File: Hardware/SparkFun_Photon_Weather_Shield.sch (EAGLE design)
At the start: 43 parts, among them U1 3.3V MIC5219, U2 HTU21D, U3 MPL3115A2LGA8

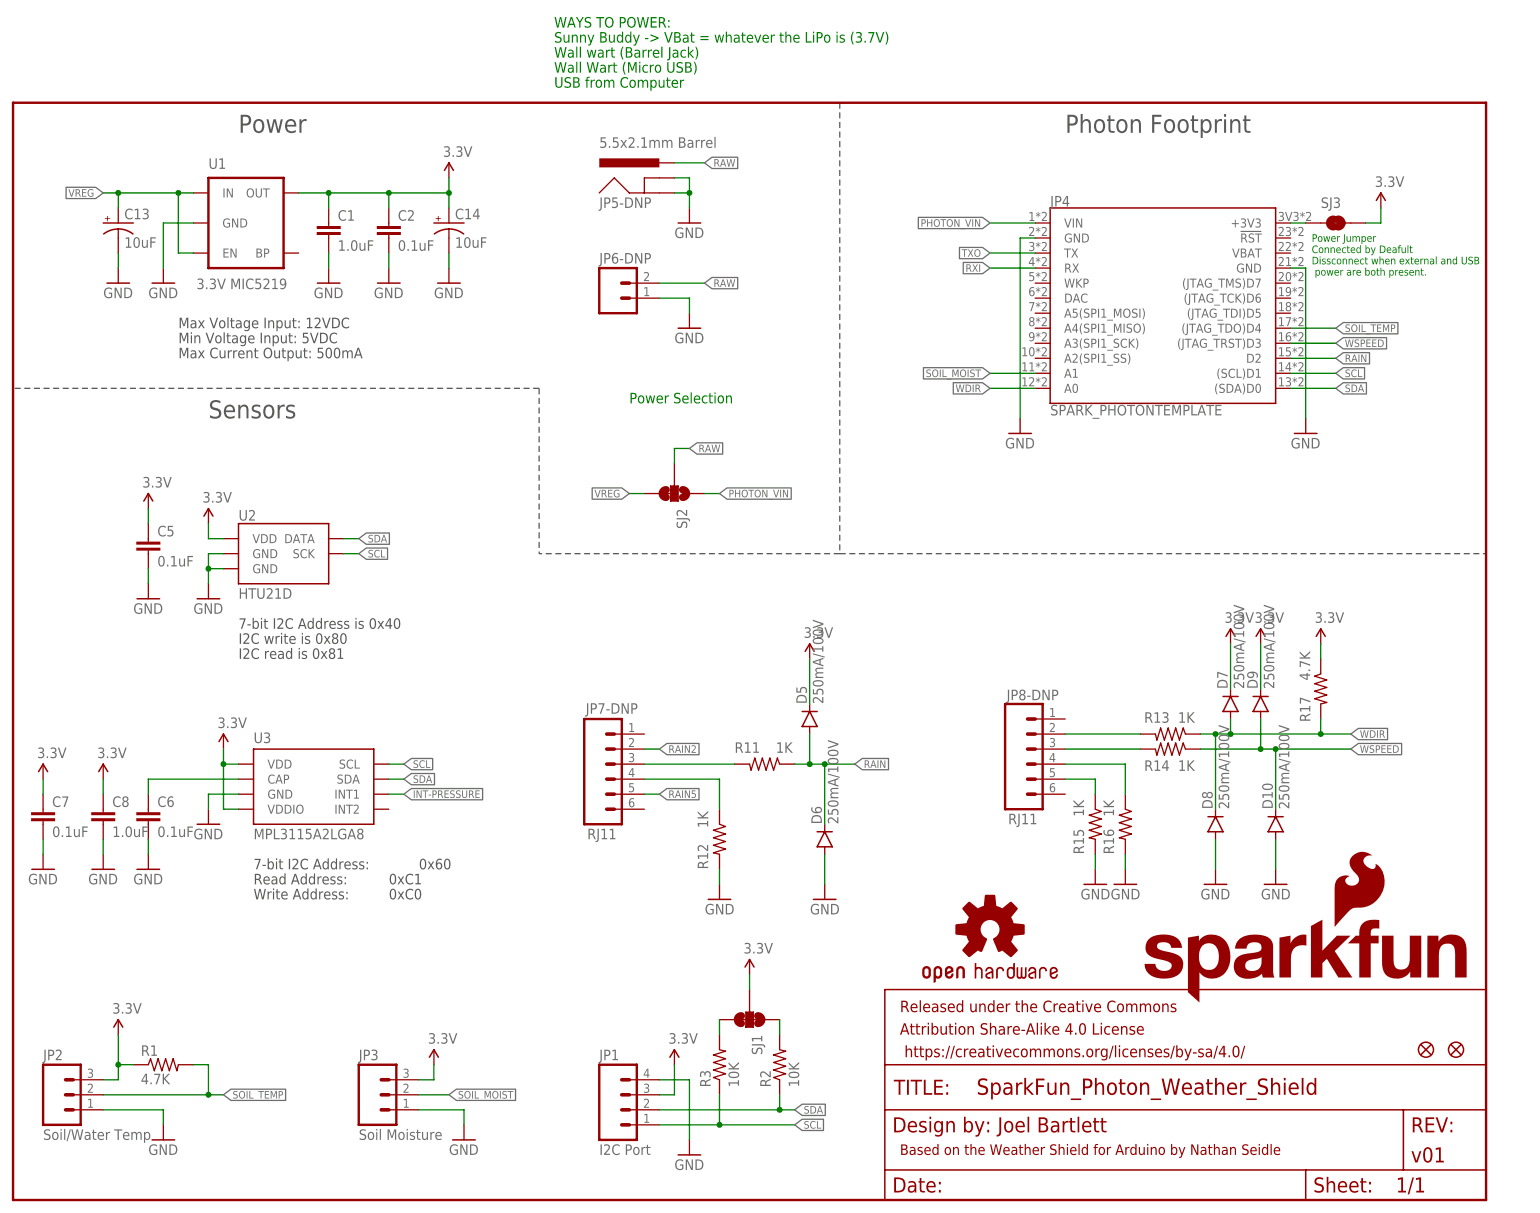
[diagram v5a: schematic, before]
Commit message: Ready for Reds
Added USART port, changed soil moisture vcc to D5, minor silk and route
changes.
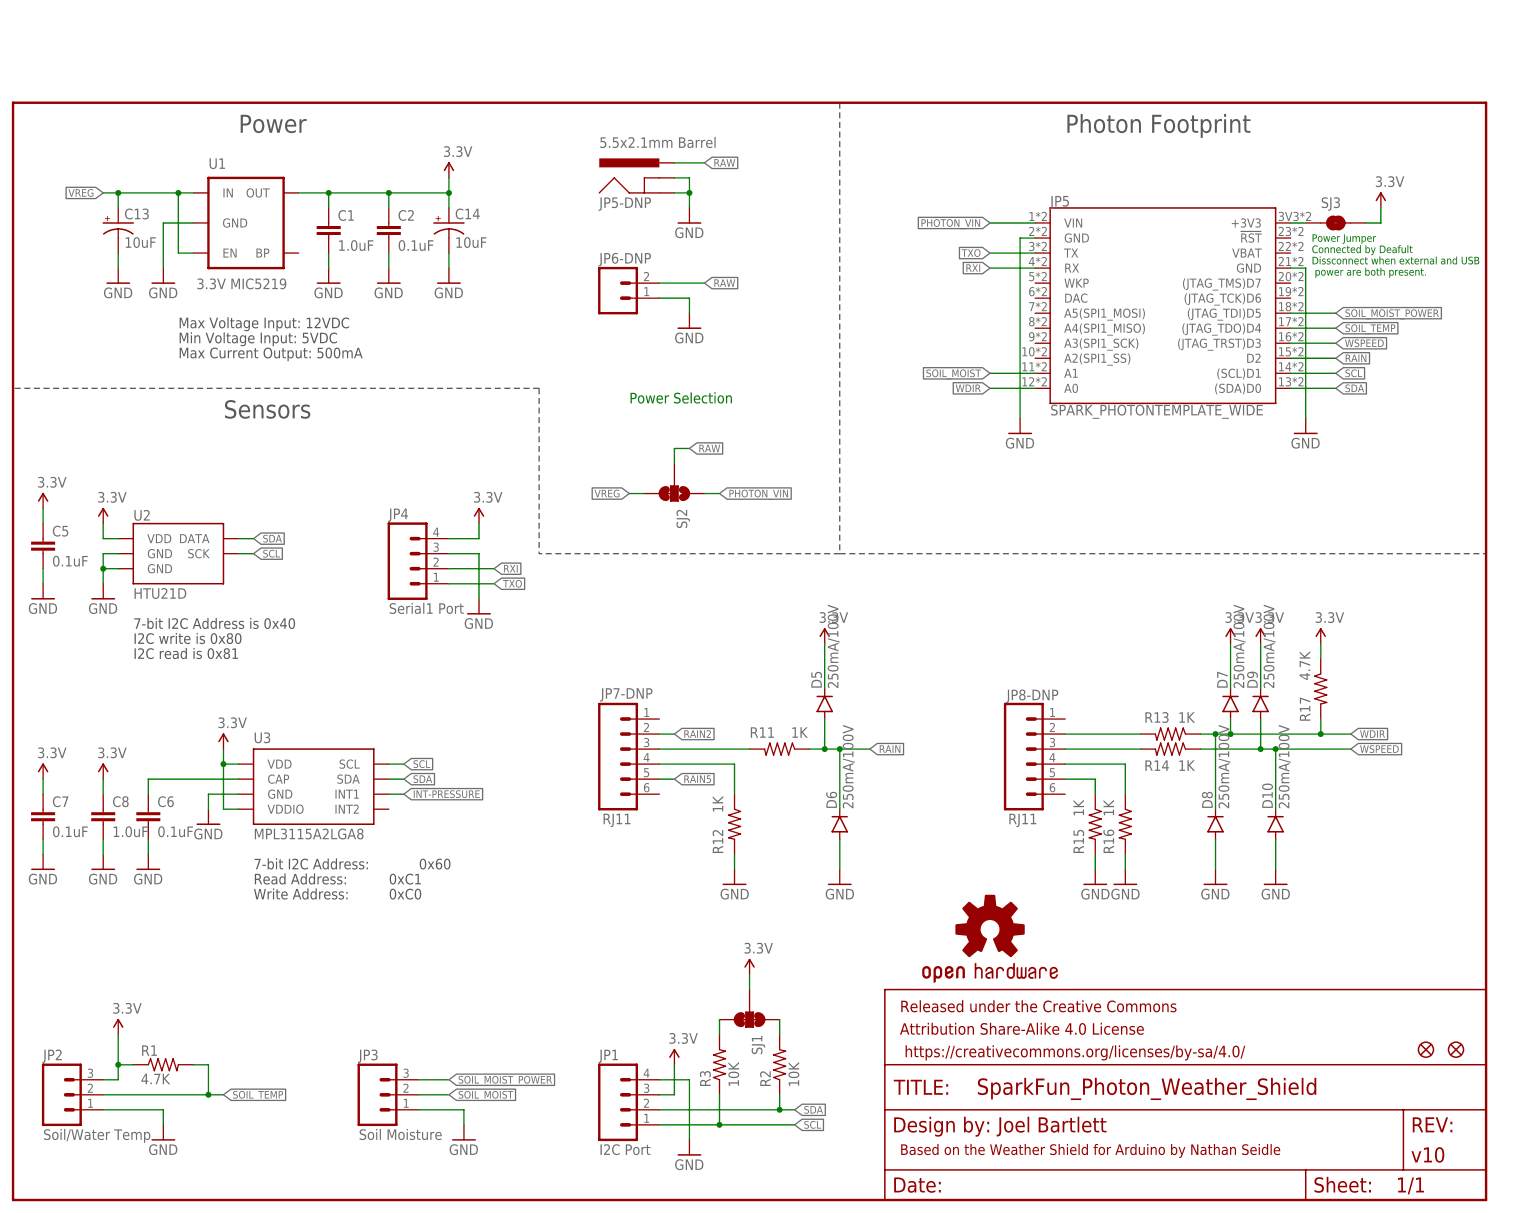
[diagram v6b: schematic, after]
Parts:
- removed LOGO2: SFE_LOGO_NAME_FLAME.1_INCH, SparkFun-Aesthetics:SFE_LOGO_NAME_FLAME.1_INCH
- added JP5: SPARK_PHOTONTEMPLATE_WIDE, template_temp:SPARK_PHOTONTEMPLATE_WIDE
- FRAME2: VERSION (none) -> v10
- JP4: value SPARK_PHOTONTEMPLATE -> Serial1 Port; device template_temp:SPARK_PHOTONTEMPLATE -> SparkFun-Connectors:M04PTH
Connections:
- new net SOIL_MOIST_POWER: JP3.3, JP5.(JTAG_TDI)D5
- net 3.3V: now also JP4.4; no longer JP3.3
- net GND: now also JP4.3, JP5.GND@2, JP5.GND@21; no longer JP4.GND@2, JP4.GND@21
- net N$7: now also JP5.+3V3; no longer JP4.+3V3
- net PHOTON_VIN: now also JP5.VIN; no longer JP4.VIN
- net RAIN: now also JP5.D2; no longer JP4.D2
- net RXI: now also JP4.2, JP5.RX; no longer JP4.RX
- net SCL: now also JP5.(SCL)D1; no longer JP4.(SCL)D1
- net SDA: now also JP5.(SDA)D0; no longer JP4.(SDA)D0
- net SOIL_MOIST: now also JP5.A1; no longer JP4.A1
- net SOIL_TEMP: now also JP5.(JTAG_TDO)D4; no longer JP4.(JTAG_TDO)D4
- net TXO: now also JP4.1, JP5.TX; no longer JP4.TX
- net WDIR: now also JP5.A0; no longer JP4.A0
- net WSPEED: now also JP5.(JTAG_TRST)D3; no longer JP4.(JTAG_TRST)D3
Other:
- note added: "Serial 1 Port (optional)"
- note removed: "Sunny Buddy -> VBat = whatever the LiPo is (3.7V)"
- note removed: "USB from Computer"
- note removed: "WAYS TO POWER:"
- note removed: "Wall Wart (Micro USB)"
- note removed: "Wall wart (Barrel Jack)"
- moved on the sheet: C5, D5, D6, JP7-DNP, R11, R12, U2

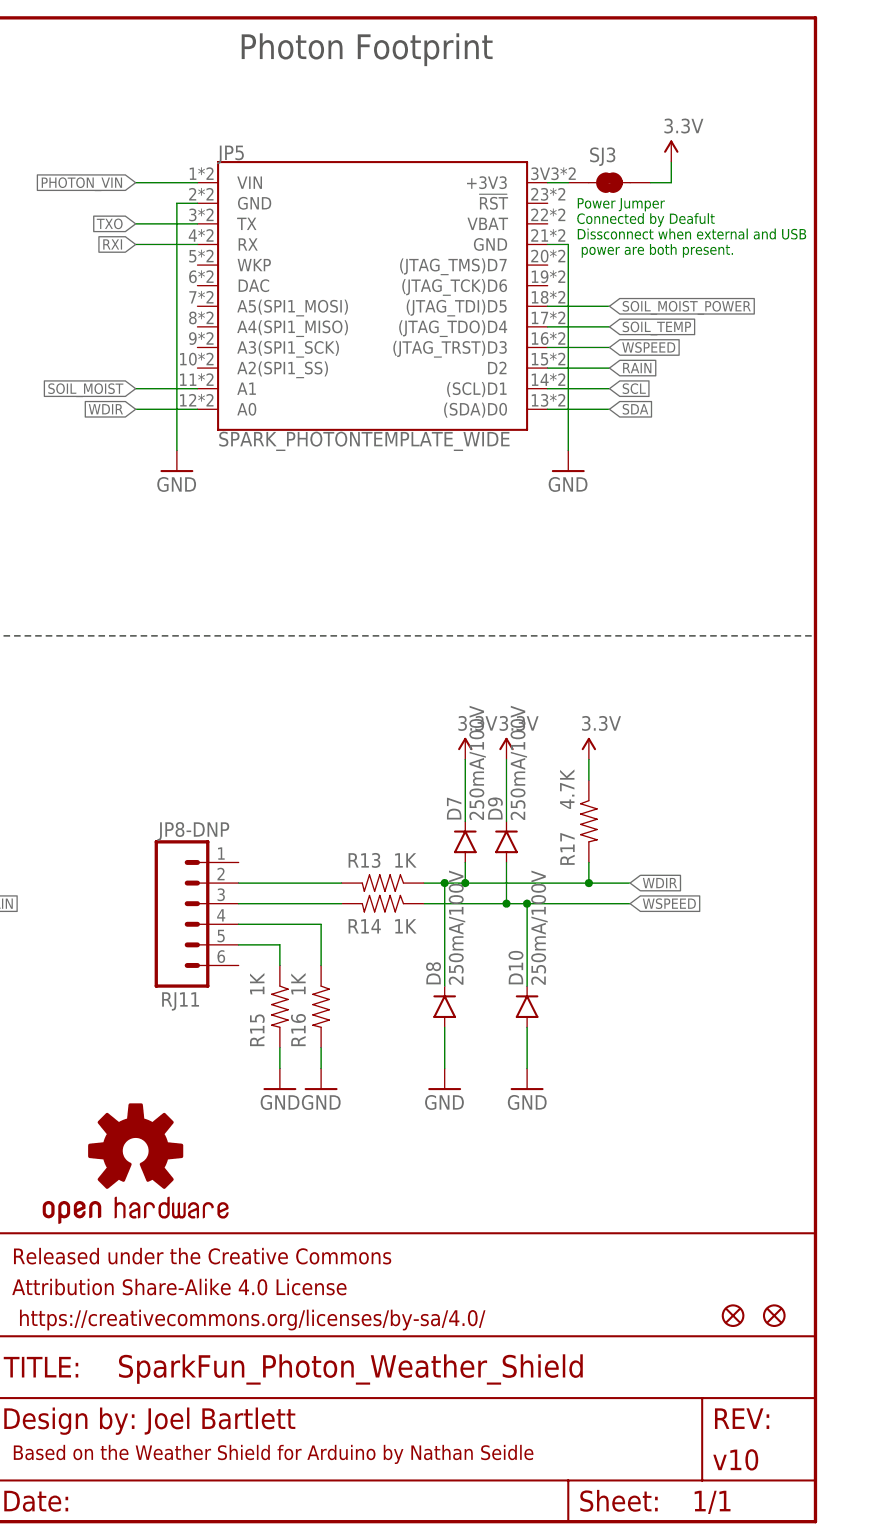
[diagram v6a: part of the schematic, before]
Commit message: Ready for last QC Check
Most recent changes pushed to github include
-Locking Footprint added to Photon Template for selective soldering
-updating Photon template to wider version for selective solder
-breakout USART port
-changing power on Soil Moisture from Vcc to D5
-Minor route and silk changes.
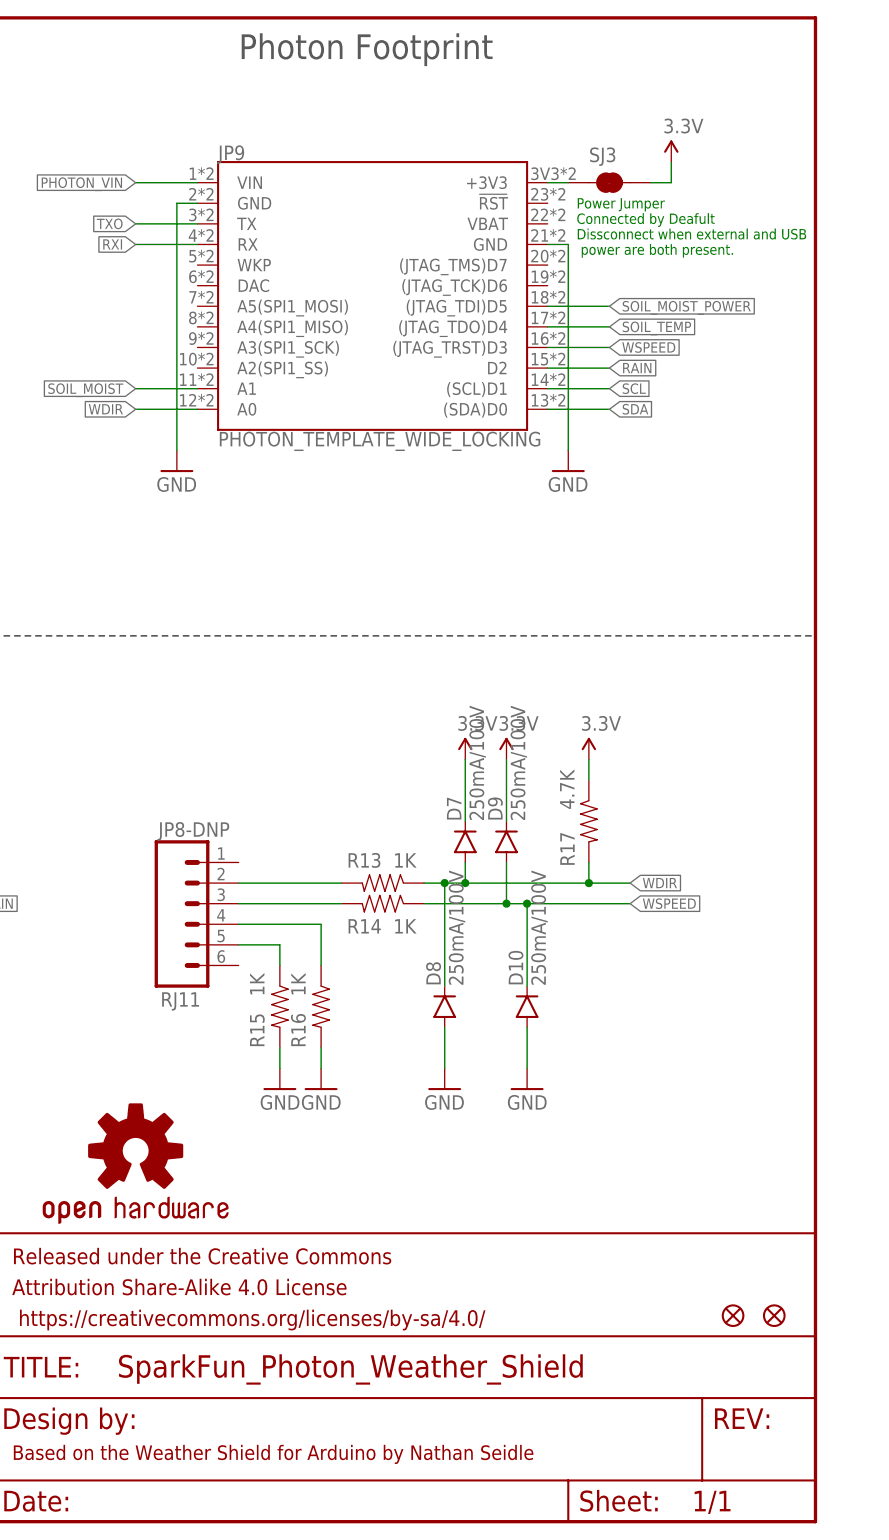
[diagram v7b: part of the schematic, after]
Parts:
- removed JP5: SPARK_PHOTONTEMPLATE_WIDE, template_temp:SPARK_PHOTONTEMPLATE_WIDE
- added JP9: PHOTON_TEMPLATE_WIDE_LOCKING, template_temp:SPARK_PHOTONSPARK_PHOTON_TEMPLATE_WIDE_LOCKING
- FRAME2: value (none) -> FRAME-LETTER; DESIGNER Joel Bartlett -> (none); VERSION v10 -> (none)
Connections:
- net GND: now also JP9.GND@2, JP9.GND@21; no longer JP5.GND@2, JP5.GND@21
- net N$7: now also JP9.+3V3; no longer JP5.+3V3
- net PHOTON_VIN: now also JP9.VIN; no longer JP5.VIN
- net RAIN: now also JP9.D2; no longer JP5.D2
- net RXI: now also JP9.RX; no longer JP5.RX
- net SCL: now also JP9.(SCL)D1; no longer JP5.(SCL)D1
- net SDA: now also JP9.(SDA)D0; no longer JP5.(SDA)D0
- net SOIL_MOIST: now also JP9.A1; no longer JP5.A1
- net SOIL_MOIST_POWER: now also JP9.(JTAG_TDI)D5; no longer JP5.(JTAG_TDI)D5
- net SOIL_TEMP: now also JP9.(JTAG_TDO)D4; no longer JP5.(JTAG_TDO)D4
- net TXO: now also JP9.TX; no longer JP5.TX
- net WDIR: now also JP9.A0; no longer JP5.A0
- net WSPEED: now also JP9.(JTAG_TRST)D3; no longer JP5.(JTAG_TRST)D3

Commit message: Ready for Reds
Ready for Reds
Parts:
- added LOGO2: SFE_LOGO_NAME.1_INCH, SparkFun-Aesthetics:SFE_LOGO_NAME.1_INCH
- renumbered FRAME2 to FRAME1, JP7-DNP to JP7, JP8-DNP to JP8
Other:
- note added: "Joel Bartlett"
- note added: "V10"
